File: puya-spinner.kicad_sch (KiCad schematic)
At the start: 2 parts

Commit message: initial sch
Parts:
- added BT1: CR2032, symbol Device:Battery_Cell
- added C1, C2, C3: 0.1 uF, symbol Device:C_Small
- added C4: 4.7 uF, symbol Device:C
- added D1, D10, D11, D12, D13, D14, D15, D16, D17, D18, D19, D2, D20, D21, D22, D23, D24, D25, D26, D27, D28, D29, D3, D30, D4, D5, D6, D7, D8, D9: RED, symbol Device:LED_Small
- added J1: Conn_ARM_SWD_TagConnect_TC2030, Connector:Tag-Connect_TC2030-IDC-FP_2x03_P1.27mm_Vertical, symbol Connector:Conn_ARM_SWD_TagConnect_TC2030
- added JP1, JP2: SolderJumper_2_Bridged, symbol Jumper:SolderJumper_2_Bridged
- added R1, R2: 10k, symbol Device:R_Small
- added R3, R4, R5, R6, R7, R8: R_Small, symbol Device:R_Small
- added TP1, TP2: TestPoint, symbol Connector:TestPoint
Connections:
- net at U2.1 (SDO): now also JP2.2 (B)
- net at U2.10 (~{CS}): now also JP1.2 (B)
- net +BATT: now reaches U2.11 (NC)
- net +BATT: now also U1.20 (VCC), U2.3 (VDDIO), U2.7 (VDD), BT1.1 (+), C1.1, C2.1, C3.1, C4.1, J1.1 (VCC), JP1.1 (A), R1.2, R2.2
- net ACCEL_SCL: now reaches U2.12 (SCx)
- net ACCEL_SCL: now also U1.9 (PF1/OSCOUT), R2.1
- net ACCEL_SDA: now reaches U2.2 (SDx)
- net ACCEL_SDA: now also U1.8 (PF0/OSCIN), R1.1
- net GND: now reaches U2.4 (NC)
- net GND: now also U1.1 (GND), U2.8 (GNDIO), U2.9 (GND), BT1.2 (-), C1.2, C2.2, C3.2, C4.2, J1.5 (GND), JP2.1 (A)
- net ACCEL_INT: now reaches U2.5 (INT1)
- net ~{RST}: now reaches U1.10 (PF2/~{RST})
- net ~{RST}: now also J1.3 (~{RESET})
- net LED_ARR_0: now reaches U1.11 (PA0)
- net LED_ARR_0: now also R3.1
- net LED_ARR_1: now reaches U1.12 (PA1)
- net LED_ARR_1: now also R4.1
- net LED_ARR_2: now reaches U1.13 (PA2)
- net LED_ARR_2: now also R5.1
- net LED_ARR_3: now reaches U1.14 (PA3)
- net LED_ARR_3: now also R6.1
- net LED_ARR_4: now reaches U1.15 (PA4)
- net LED_ARR_4: now also R7.1
- net DBG_RX: now reaches U1.18 (PB2)
- net DBG_RX: now also TP2.1
- net SWDIO: now reaches U1.2 (PA13/SWD)
- net SWDIO: now also J1.2 (SWDIO)
- net SWCLK: now reaches U1.3 (PA14/SWC)
- net SWCLK: now also J1.4 (SWCLK)
- net BOOT0_DBG_TX: now reaches U1.5 (PB6/PF4/BOOT0)
- net BOOT0_DBG_TX: now also TP1.1
- net LED_ARR_5: now reaches U1.7 (PA5)
- net LED_ARR_5: now also R8.1
- new net: D1.1 (K), D10.2 (A), D15.2 (A), D2.1 (K), D20.2 (A), D25.2 (A), D3.1 (K), D30.2 (A), D4.1 (K), D5.1 (K), R8.2
- new net: D1.2 (A), D11.2 (A), D16.2 (A), D21.2 (A), D26.1 (K), D27.1 (K), D28.1 (K), D29.1 (K), D30.1 (K), D6.2 (A), R3.2
- new net: D10.1 (K), D14.2 (A), D19.2 (A), D24.2 (A), D29.2 (A), D5.2 (A), D6.1 (K), D7.1 (K), D8.1 (K), D9.1 (K), R7.2
- new net: D12.2 (A), D17.2 (A), D2.2 (A), D21.1 (K), D22.1 (K), D23.1 (K), D24.1 (K), D25.1 (K), D26.2 (A), D7.2 (A), R4.2
- new net: D13.2 (A), D16.1 (K), D17.1 (K), D18.1 (K), D19.1 (K), D20.1 (K), D22.2 (A), D27.2 (A), D3.2 (A), D8.2 (A), R5.2
- new net: D11.1 (K), D12.1 (K), D13.1 (K), D14.1 (K), D15.1 (K), D18.2 (A), D23.2 (A), D28.2 (A), D4.2 (A), D9.2 (A), R6.2
- no-connect marks 0 -> 7
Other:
- note added: "always i2c mode"
- note added: "can be used to flip boot0 (maybe?) can be used as debug uart tx"
- note added: "xxx how does tying SDO low for address selection work exactly?"
- note added: "xxx why are the NC pins connected??"
- moved on the sheet: U1, U2

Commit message: assign most parts
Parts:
- C1, C2, C3: footprint (none) -> Capacitor_SMD:C_0402_1005Metric; LCSC (none) -> C1525
- C4: value 4.7 uF -> 10 uF; footprint (none) -> Capacitor_SMD:C_1206_3216Metric; LCSC (none) -> C13585
- D1, D10, D11, D12, D13, D14, D15, D16, D17, D18, D19, D2, D20, D21, D22, D23, D24, D25, D26, D27, D28, D29, D3, D30, D4, D5, D6, D7, D8, D9: footprint (none) -> LED_SMD:LED_0603_1608Metric; LCSC (none) -> C2286
- JP1, JP2: footprint (none) -> Jumper:SolderJumper-2_P1.3mm_Bridged_RoundedPad1.0x1.5mm
- R1, R2: footprint (none) -> Resistor_SMD:R_0402_1005Metric; LCSC (none) -> C25744
- R3, R4, R5, R6, R7, R8: value R_Small -> 100; footprint (none) -> Resistor_SMD:R_0402_1005Metric; LCSC (none) -> C25076
- TP1, TP2: footprint (none) -> TestPoint:TestPoint_Pad_2.0x2.0mm
- U1: value ~ -> PY32F002AF15P6; footprint (none) -> Package_SO:TSSOP-20_4.4x6.5mm_P0.65mm; LCSC (none) -> C5292059
- U2: value ~ -> SC7A20; footprint (none) -> Package_LGA:LGA-12_2x2mm_P0.5mm; LCSC (none) -> C5126709
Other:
- moved on the sheet: BT1, C1, C2, C3, C4, D1, D10, D11, D12, D13, D14, D15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

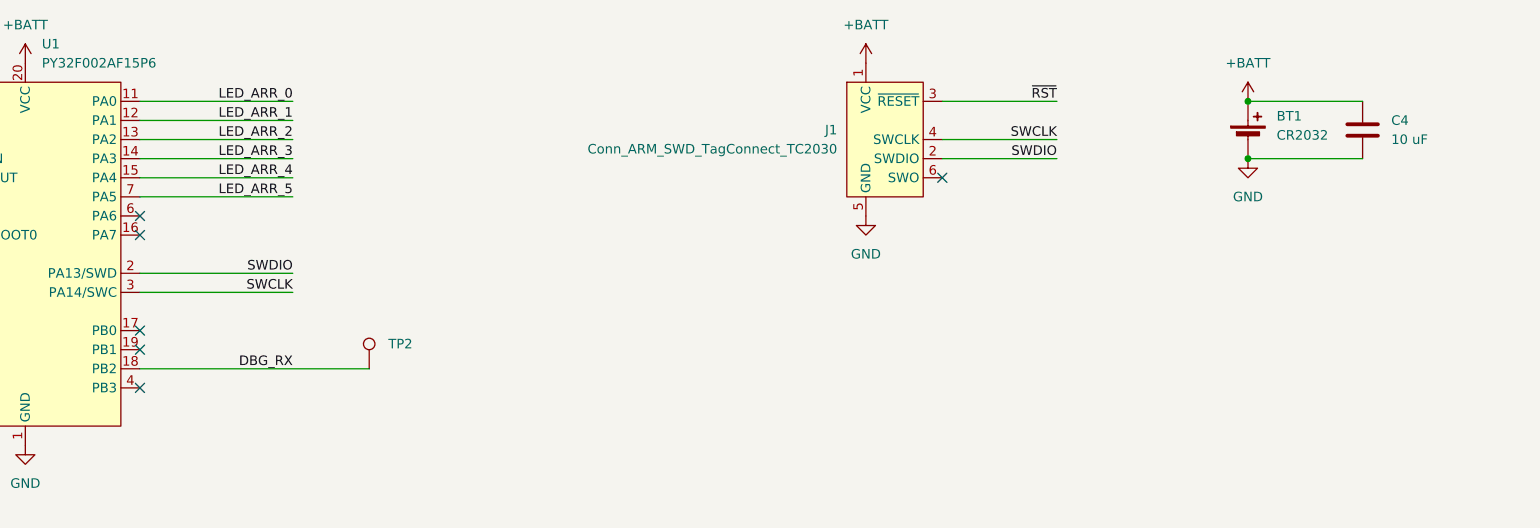
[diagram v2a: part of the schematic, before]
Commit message: add power flags; fix interrupt pin
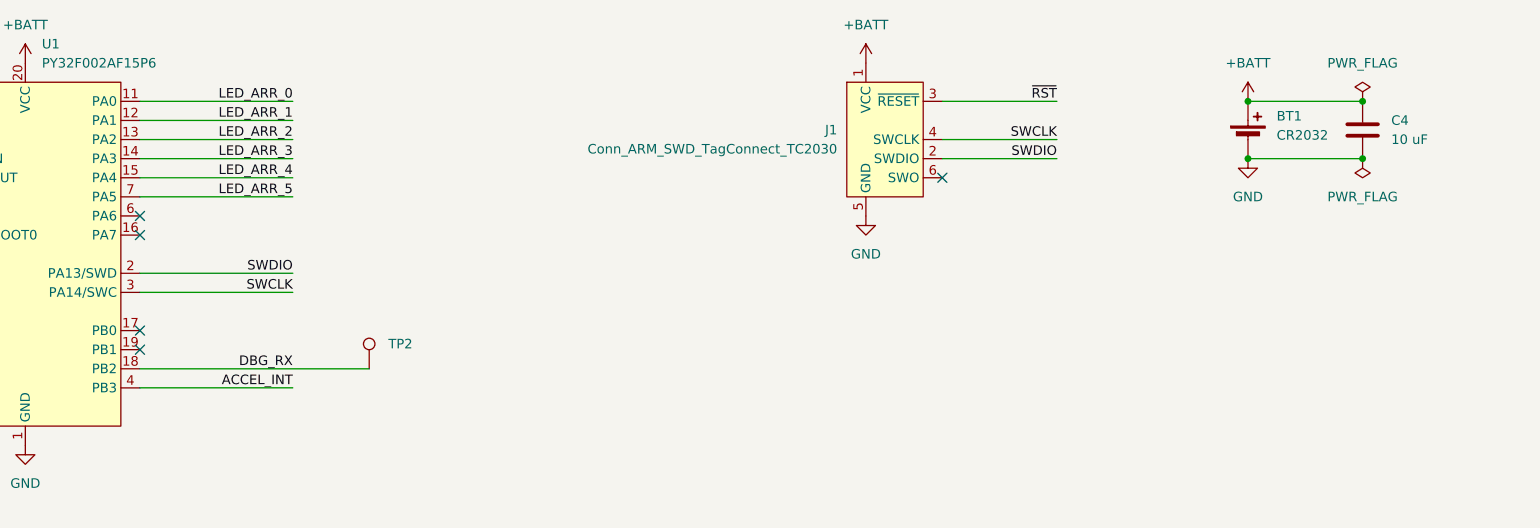
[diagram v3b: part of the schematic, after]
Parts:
- BT1: footprint (none) -> parts:Battery_MYOUNG_BS-07-A1BJ001_CR2032
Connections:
- net ACCEL_INT: now also U1.4 (PB3)
- no-connect marks 7 -> 6
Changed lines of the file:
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@@
 	)
 	(junction
+		(at 243.84 33.02)
+		(diameter 0)
+		(color 0 0 0 0)
+	)
+	(junction
 		(at 228.6 111.76)
 		(diameter 0)
@@
 	)
 	(junction
+		(at 243.84 25.4)
+		(diameter 0)
+		(color 0 0 0 0)
+	)
+	(junction
 		(at 26.67 177.8)
 		(diameter 0)
@@
 	)
 	(no_connect
-		(at 81.28 63.5)
-	)
-	(no_connect
 		(at 81.28 58.42)
 	)
@@
 	(wire
 		(pts
+			(xy 81.28 63.5) (xy 101.6 63.5)
+		)
+		(stroke
+			(width 0)
+			(type default)
+		)
+	)
+	(wire
+		(pts
 			(xy 259.08 127) (xy 259.08 139.7)
 		)
@@
 		)
 	)
+	(label "ACCEL_INT"
+		(at 101.6 63.5 180)
+		(fields_autoplaced yes)
+		(effects
+			(font
+				(size 1.27 1.27)
+			)
+			(justify right bottom)
+		)
+	)
 	(label "LED_ARR_1"
 		(at 101.6 27.94 180)
@@
 			)
 		)
-		(property "Footprint" ""
+		(property "Footprint" "parts:Battery_MYOUNG_BS-07-A1BJ001_CR2032"
 			(at 228.6 28.956 90)
 			(effects
@@
 	)
 	(symbol
+		(lib_id "power:PWR_FLAG")
+		(at 243.84 33.02 180)
+		(unit 1)
+		(exclude_from_sim no)
+		(in_bom yes)
+		(on_board yes)
+		(dnp no)
+		(fields_autoplaced yes)
+		(property "Reference" "#FLG02"
+			(at 243.84 34.925 0)
+			(effects
+				(font
+					(size 1.27 1.27)
+				)
+				(hide yes)
+			)
+		)
+		(property "Value" "PWR_FLAG"
+			(at 243.84 38.1 0)
+			(effects
+				(font
+					(size 1.27 1.27)
+				)
+			)
+		)
+		(property "Footprint" ""
+			(at 243.84 33.02 0)
+			(effects
+				(font
+					(size 1.27 1.27)
+				)
+				(hide yes)
+			)
+		)
+		(property "Datasheet" "~"
+			(at 243.84 33.02 0)
+			(effects
+				(font
+					(size 1.27 1.27)
+				)
+				(hide yes)
+			)
+		)
+		(property "Description" "Special symbol for telling ERC where power comes from"
+			(at 243.84 33.02 0)
+			(effects
+				(font
+					(size 1.27 1.27)
+				)
+				(hide yes)
+			)
+		)
+		(pin "1"
+		)
+		(instances
+			(project "puya-spinner"
+				(path "/55924447-94dd-4524-a9d3-3f79a9e023c8"
+					(reference "#FLG02")
+					(unit 1)
+				)
+			)
+		)
+	)
+	(symbol
 		(lib_id "Device:C")
 		(at 243.84 29.21 0)
@@
 					(unit 1)
 				)
+			)
+		)
+	)
+	(symbol
+		(lib_id "power:PWR_FLAG")
+		(at 243.84 25.4 0)
+		(unit 1)
+		(exclude_from_sim no)
+		(in_bom yes)
+		(on_board yes)
+		(dnp no)
+		(fields_autoplaced yes)
+		(property "Reference" "#FLG01"
+			(at 243.84 23.495 0)
+			(effects
+				(font
+					(size 1.27 1.27)
+				)
+				(hide yes)
+			)
+		)
+		(property "Value" "PWR_FLAG"
+			(at 243.84 20.32 0)
+			(effects
+				(font
+					(size 1.27 1.27)
+				)
+			)
+		)
+		(property "Footprint" ""
+			(at 243.84 25.4 0)
+			(effects
+				(font
+					(size 1.27 1.27)
+				)
+				(hide yes)
+			)
+		)
+		(property "Datasheet" "~"
+			(at 243.84 25.4 0)
+			(effects
+				(font
+					(size 1.27 1.27)
+				)
+				(hide yes)
+			)
+		)
+		(property "Description" "Special symbol for telling ERC where power comes from"
+			(at 243.84 25.4 0)
+			(effects
+				(font
+					(size 1.27 1.27)
+				)
+				(hide yes)
+			)
+		)
+		(pin "1"
+		)
+		(instances
+			(project "puya-spinner"
+				(path "/55924447-94dd-4524-a9d3-3f79a9e023c8"
+					(reference "#FLG01")
+					(unit 1)
+				)
